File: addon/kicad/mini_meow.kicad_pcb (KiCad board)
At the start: 2 copper layers, 5 parts, among them U1 sa_connector

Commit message: pcb update, added working art files
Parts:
- added G***: LOGO, mini_meow:mini_meow_silk_lg, F.Cu at (152.2, 88.9)
- moved R1 126.5 mm to (245.0, 92.5)
- moved D1 121.1 mm to (245.0, 80.0)
- moved D2 115.1 mm to (222.5, 77.5)
- moved U1 110.8 mm to (230.0, 90.0)
- moved R2 107.3 mm to (220.0, 92.5)
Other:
- board outline added: 128.7 x 63.4 mm
- net class Default: clearance 0.2 -> 0.254; trace_width 0.25 -> 0.254; via_dia 0.6 -> 0.6858; via_drill 0.4 -> 0.3302
- rule trace_clearance: 0.2 -> 0.254

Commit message: updated library, added copper images
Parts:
- added G***: LOGO, mini_meow:mini_meow_nose, F.Cu at (148.7, 85.6)
- added G***: LOGO, mini_meow:mini_meow_necklace, F.Cu at (148.4, 99.8)
- added G***: LOGO, mini_meow:mini_meow_belly, F.Cu at (148.8, 114.0)
- moved D1 88.3 mm to (156.8, 80.7), turned to 0 degrees
- moved R2 86.3 mm to (133.7, 90.0), turned to 0 degrees
- moved D2 81.8 mm to (140.8, 80.7)
- moved U1 80.5 mm to (150.0, 99.0), turned to 180 degrees
- moved R1 80.4 mm to (164.6, 90.2), turned to 180 degrees
- moved G*** 0.18 mm to (152.1, 88.8)
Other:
- board size 128.7 x 63.4 mm -> 49.3 x 63.4 mm

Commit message: updated pcb, maybe first final draft
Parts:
- D1, D2, R1, R2, U1: moved to B.Cu
- moved R2 30.9 mm to (134.1, 120.9)
- moved R1 30.7 mm to (163.6, 120.9)
- moved U1 0.62 mm to (150.4, 98.6)
- moved G*** 0.43 mm to (148.8, 99.6)
- moved D1 0.31 mm to (156.5, 80.8)
- moved D2 0.15 mm to (140.7, 80.8)
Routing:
- net Net-(D1-Pad2): track 0.00 -> 42.2 mm
- net Net-(D2-Pad2): track 0.00 -> 41.8 mm
- net +3V3: track 0.00 -> 41.0 mm
- added copper zone on B.Cu, net GND
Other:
- board text added: "Y2F0cyBkb24ndCBoYXZlIFIxMyBsaXZlcw=="
- board text added: "dash"
- board text added: "defcon26-meow"
- board text added: "nekosurf <3"
- board text added: "tense future"

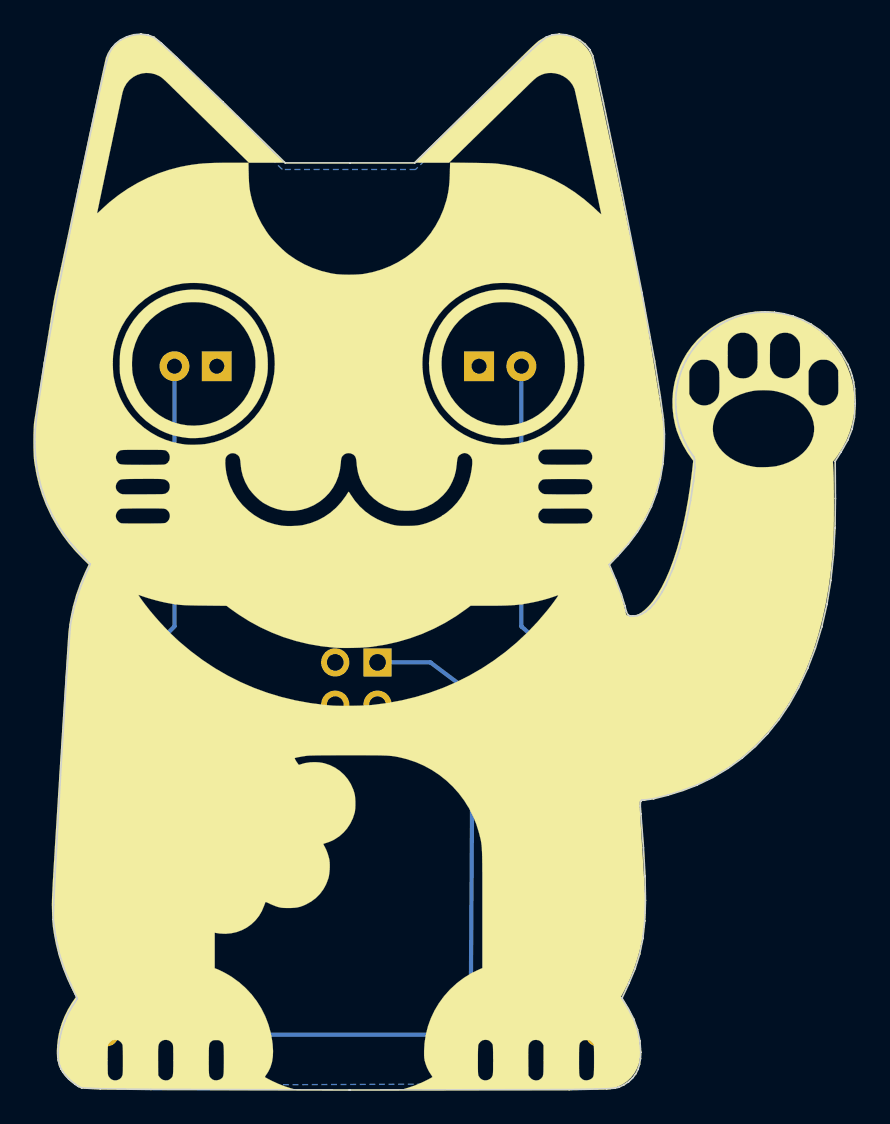
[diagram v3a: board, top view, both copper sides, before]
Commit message: updated copper layers. added ground
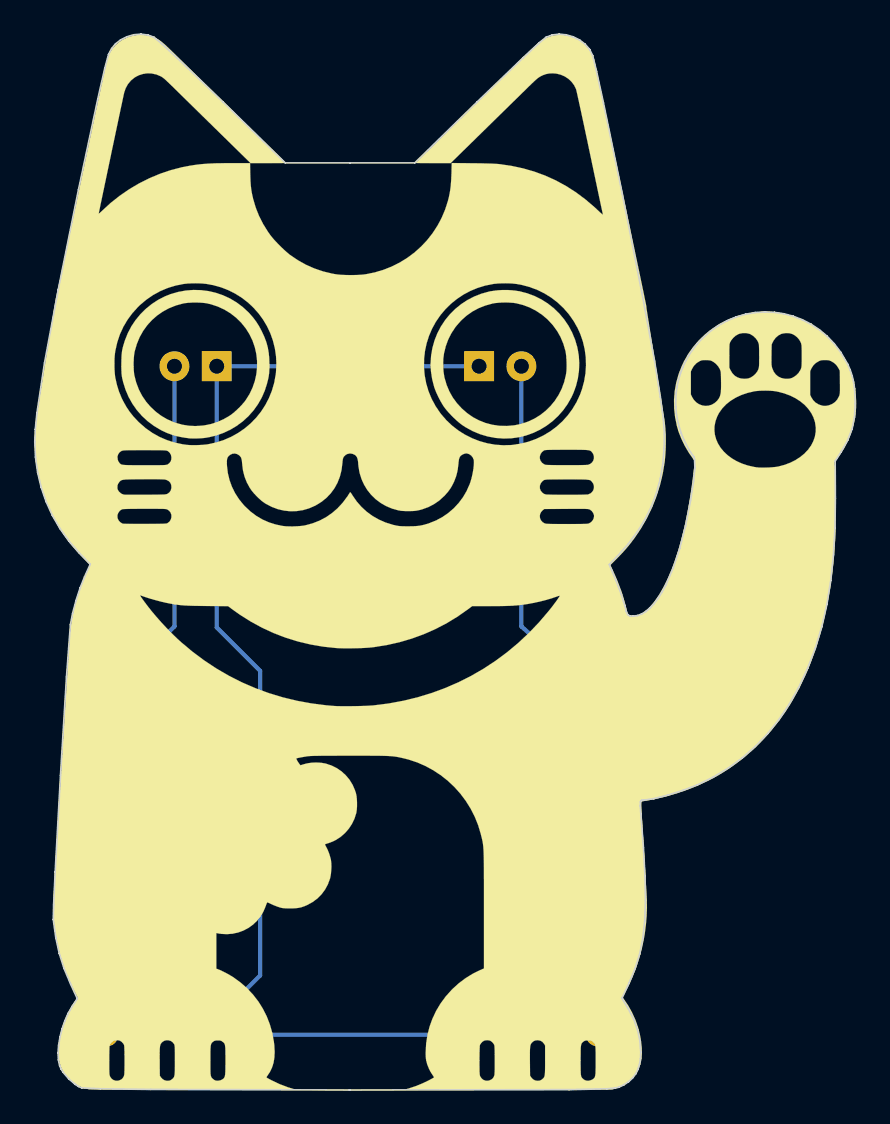
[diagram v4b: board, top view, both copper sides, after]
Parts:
- added G***: LOGO, mini_meow:heart, B.Cu at (173.6, 82.8)
- moved U1 13.7 mm to (143.3, 110.3), turned to 90 degrees
- moved G*** 1.08 mm to (148.9, 98.5)
- moved G*** 0.10 mm to (152.1, 88.8)
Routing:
- net GND: track 0.00 -> 43.8 mm
- net +3V3: track 41.0 -> 25.6 mm
- removed copper zone on B.Cu, net GND
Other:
- board text added: "nekosurf"
- board text removed: "nekosurf <3"

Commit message: updated copper layers....again...
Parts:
- moved G*** 1.13 mm to (149.2, 99.6), turned to 0 degrees
- moved G*** 0.21 mm to (149.0, 114.1)
- moved G*** 0.19 mm to (148.7, 85.4)
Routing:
- net GND: track 43.8 -> 67.9 mm
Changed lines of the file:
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@@
     (thickness 1.6)
     (drawings 221)
-    (tracks 18)
+    (tracks 20)
     (zones 0)
     (modules 10)
@@
       (xy 5.695666 -12.574343) (xy 6.06983 -12.573966)) (layer F.SilkS) (width 0.01))
   )
+  (module mini_meow:heart (layer B.Cu)
+    (at 173.609 82.804 180)
+    (fp_text reference G*** (at 0 0 180) (layer B.SilkS) hide
+      (effects (font (thickness 0.3)) (justify mirror))
+    )
+    (fp_text value LOGO (at 0.75 0 180) (layer B.SilkS) hide
+      (effects (font (thickness 0.3)) (justify mirror))
+    )
+    (fp_poly (pts (xy -0.690576 1.381518) (xy -0.548786 1.307765) (xy -0.402225 1.189289) (xy -0.344715 1.133323)
+      (xy -0.259095 1.042376) (xy -0.180277 0.951003) (xy -0.120334 0.873512) (xy -0.101701 0.845269)
+      (xy -0.062368 0.783353) (xy -0.033115 0.74457) (xy -0.024851 0.738021) (xy -0.00569 0.757723)
+      (xy 0.026022 0.807777) (xy 0.037334 0.828133) (xy 0.095374 0.913847) (xy 0.182086 1.015689)
+      (xy 0.285558 1.122043) (xy 0.393877 1.221293) (xy 0.495128 1.301823) (xy 0.572072 1.349525)
+      (xy 0.725984 1.398362) (xy 0.896095 1.410114) (xy 1.063644 1.384625) (xy 1.148611 1.35436)
+      (xy 1.287825 1.271329) (xy 1.421227 1.154973) (xy 1.531617 1.021525) (xy 1.572276 0.954474)
+      (xy 1.604083 0.888798) (xy 1.623999 0.828108) (xy 1.634662 0.757292) (xy 1.63871 0.661238)
+      (xy 1.639024 0.572072) (xy 1.635808 0.435182) (xy 1.625575 0.33177) (xy 1.605799 0.244661)
+      (xy 1.580147 0.171989) (xy 1.514945 0.030874) (xy 1.430264 -0.110054) (xy 1.322391 -0.254857)
+      (xy 1.187612 -0.407599) (xy 1.022212 -0.572343) (xy 0.822479 -0.753152) (xy 0.584697 -0.954089)
+      (xy 0.452692 -1.061512) (xy 0.322737 -1.165479) (xy 0.205672 -1.257791) (xy 0.10737 -1.333926)
+      (xy 0.033705 -1.389363) (xy -0.00945 -1.41958) (xy -0.017888 -1.423824) (xy -0.04415 -1.408527)
+      (xy -0.101634 -1.366604) (xy -0.182515 -1.304006) (xy -0.27897 -1.226685) (xy -0.305357 -1.205132)
+      (xy -0.435211 -1.098634) (xy -0.580722 -0.979255) (xy -0.722323 -0.86305) (xy -0.820734 -0.782262)
+      (xy -1.091811 -0.54456) (xy -1.313706 -0.316532) (xy -1.48693 -0.097062) (xy -1.611993 0.114969)
+      (xy -1.689408 0.320679) (xy -1.719683 0.521186) (xy -1.703329 0.717608) (xy -1.640858 0.911063)
+      (xy -1.617034 0.961194) (xy -1.538656 1.079617) (xy -1.431385 1.193412) (xy -1.310361 1.288975)
+      (xy -1.190725 1.352701) (xy -1.175169 1.358235) (xy -0.994982 1.404374) (xy -0.83638 1.412928)
+      (xy -0.690576 1.381518)) (layer B.Mask) (width 0.01))
+  )
   (module mini_meow:mini_meow_nose (layer F.Cu)
-    (at 148.7 85.6)
-    (fp_text reference G*** (at 0 0) (layer F.SilkS) hide
+    (at 148.717 85.4075)
+    (fp_text reference G*** (at 0 0) (layer F.Cu) hide
       (effects (font (thickness 0.3)))
     )
-    (fp_text value LOGO (at 0.75 0) (layer F.SilkS) hide
+    (fp_text value LOGO (at 0.75 0) (layer F.Cu) hide
       (effects (font (thickness 0.3)))
     )
@@
       (xy -1.924858 -1.183145) (xy -1.841776 -1.186452) (xy -1.735622 -1.189068) (xy -1.602989 -1.191076)
       (xy -1.440471 -1.192555) (xy -1.24466 -1.193587) (xy -1.012151 -1.194252) (xy -0.739536 -1.194632)
-      (xy -0.423409 -1.194807) (xy -0.060363 -1.194858) (xy 0 -1.19486) (xy 0.372186 -1.194811)) (layer F.Mask) (width 0.01))
+      (xy -0.423409 -1.194807) (xy -0.060363 -1.194858) (xy 0 -1.19486) (xy 0.372186 -1.194811)) (layer F.Cu) (width 0.01))
   )
   (module mini_meow:mini_meow_necklace (layer F.Cu)
-    (at 148.9075 98.4885 90)
-    (fp_text reference G*** (at 0 0 90) (layer F.SilkS) hide
+    (at 149.225 99.568)
+    (fp_text reference G*** (at 0 0) (layer F.Cu) hide
       (effects (font (thickness 0.3)))
     )
-    (fp_text value LOGO (at 0.75 0 90) (layer F.SilkS) hide
+    (fp_text value LOGO (at 0.75 0) (layer F.Cu) hide
       (effects (font (thickness 0.3)))
     )
@@
       (xy -2.289693 -2.215709) (xy -1.991288 -2.488926) (xy -1.667949 -2.719084) (xy -1.323118 -2.905262)
       (xy -0.960235 -3.04654) (xy -0.582738 -3.141996) (xy -0.19407 -3.19071) (xy 0.202331 -3.19176)
-      (xy 0.603024 -3.144227)) (layer F.Mask) (width 0.01))
+      (xy 0.603024 -3.144227)) (layer F.Cu) (width 0.01))
   )
   (module mini_meow:mini_meow_belly (layer F.Cu)
-    (at 148.85 114)
-    (fp_text reference G*** (at 0 0) (layer F.SilkS) hide
+    (at 149.0345 114.1095)
+    (fp_text reference G*** (at 0 0) (layer F.Cu) hide
       (effects (font (thickness 0.3)))
     )
-    (fp_text value LOGO (at 0.75 0) (layer F.SilkS) hide
+    (fp_text value LOGO (at 0.75 0) (layer F.Cu) hide
       (effects (font (thickness 0.3)))
     )
@@
       (xy -2.798548 -9.833833) (xy -2.656381 -9.853188) (xy -2.555255 -9.865327) (xy -2.477675 -9.871066)
       (xy -2.356242 -9.875898) (xy -2.190114 -9.879831) (xy -1.978447 -9.882872) (xy -1.720399 -9.885025)
-      (xy -1.415128 -9.886298) (xy -1.061791 -9.886698) (xy -0.659546 -9.88623)) (layer F.Mask) (width 0.01))
-  )
-  (module mini_meow:heart (layer B.Cu)
-    (at 173.609 82.804 180)
-    (fp_text reference G*** (at 0 0 180) (layer B.SilkS) hide
-      (effects (font (thickness 0.3)) (justify mirror))
-    )
-    (fp_text value LOGO (at 0.75 0 180) (layer B.SilkS) hide
-      (effects (font (thickness 0.3)) (justify mirror))
-    )
-    (fp_poly (pts (xy -0.690576 1.381518) (xy -0.548786 1.307765) (xy -0.402225 1.189289) (xy -0.344715 1.133323)
-      (xy -0.259095 1.042376) (xy -0.180277 0.951003) (xy -0.120334 0.873512) (xy -0.101701 0.845269)
-      (xy -0.062368 0.783353) (xy -0.033115 0.74457) (xy -0.024851 0.738021) (xy -0.00569 0.757723)
-      (xy 0.026022 0.807777) (xy 0.037334 0.828133) (xy 0.095374 0.913847) (xy 0.182086 1.015689)
-      (xy 0.285558 1.122043) (xy 0.393877 1.221293) (xy 0.495128 1.301823) (xy 0.572072 1.349525)
-      (xy 0.725984 1.398362) (xy 0.896095 1.410114) (xy 1.063644 1.384625) (xy 1.148611 1.35436)
-      (xy 1.287825 1.271329) (xy 1.421227 1.154973) (xy 1.531617 1.021525) (xy 1.572276 0.954474)
-      (xy 1.604083 0.888798) (xy 1.623999 0.828108) (xy 1.634662 0.757292) (xy 1.63871 0.661238)
-      (xy 1.639024 0.572072) (xy 1.635808 0.435182) (xy 1.625575 0.33177) (xy 1.605799 0.244661)
-      (xy 1.580147 0.171989) (xy 1.514945 0.030874) (xy 1.430264 -0.110054) (xy 1.322391 -0.254857)
-      (xy 1.187612 -0.407599) (xy 1.022212 -0.572343) (xy 0.822479 -0.753152) (xy 0.584697 -0.954089)
-      (xy 0.452692 -1.061512) (xy 0.322737 -1.165479) (xy 0.205672 -1.257791) (xy 0.10737 -1.333926)
-      (xy 0.033705 -1.389363) (xy -0.00945 -1.41958) (xy -0.017888 -1.423824) (xy -0.04415 -1.408527)
-      (xy -0.101634 -1.366604) (xy -0.182515 -1.304006) (xy -0.27897 -1.226685) (xy -0.305357 -1.205132)
-      (xy -0.435211 -1.098634) (xy -0.580722 -0.979255) (xy -0.722323 -0.86305) (xy -0.820734 -0.782262)
-      (xy -1.091811 -0.54456) (xy -1.313706 -0.316532) (xy -1.48693 -0.097062) (xy -1.611993 0.114969)
-      (xy -1.689408 0.320679) (xy -1.719683 0.521186) (xy -1.703329 0.717608) (xy -1.640858 0.911063)
-      (xy -1.617034 0.961194) (xy -1.538656 1.079617) (xy -1.431385 1.193412) (xy -1.310361 1.288975)
-      (xy -1.190725 1.352701) (xy -1.175169 1.358235) (xy -0.994982 1.404374) (xy -0.83638 1.412928)
-      (xy -0.690576 1.381518)) (layer B.Mask) (width 0.01))
+      (xy -1.415128 -9.886298) (xy -1.061791 -9.886698) (xy -0.659546 -9.88623)) (layer F.Cu) (width 0.01))
   )
   (gr_text Y2F0cyBkb24ndCBoYXZlIFIxMyBsaXZlcw== (at 148.336 74.422) (layer B.SilkS)
@@
   (gr_line (start 132.41897 124.01002) (end 132.220026 123.884121) (layer Edge.Cuts) (width 0.1))
   (gr_line (start 132.607035 124.095547) (end 132.41897 124.01002) (layer Edge.Cuts) (width 0.1))
-  (segment (start 156.464 80.772) (end 140.716 80.772) (width 0.254) (layer B.Cu) (net 1))
+  (segment (start 156.464 80.772) (end 156.083 107.823) (width 0.254) (layer B.Cu) (net 1))
+  (segment (start 145.161 107.7595) (end 143.3195 107.7595) (width 0.254) (layer B.Cu) (net 1))
+  (segment (start 156.083 107.823) (end 145.161 107.7595) (width 0.254) (layer B.Cu) (net 1))
   (segment (start 140.716 80.772) (end 140.716 96.4565) (width 0.254) (layer B.Cu) (net 1))
   (segment (start 143.3195 99.06) (end 143.3195 107.7595) (width 0.254) (layer B.Cu) (net 1))

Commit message: updated some silkscreen text
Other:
- board text added: "+"
- board text added: "-"
- board text added: "GND"
- board text added: "MEOW EMWO OWME WOEM"
- board text added: "VCC"
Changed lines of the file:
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@@
     (links 6)
     (no_connects 0)
-    (area 129.545923 60.619632 179.358787 124.630237)
+    (area 129.545923 60.619632 179.358787 124.739737)
     (thickness 1.6)
-    (drawings 221)
+    (drawings 228)
     (tracks 20)
     (zones 0)
@@
   (page A4)
   (layers
-    (0 F.Cu signal)
+    (0 F.Cu signal hide)
     (31 B.Cu signal)
     (32 B.Adhes user)
@@
     (descr "LED, diameter 5.0mm, 2 pins, http://cdn-reichelt.de/documents/datenblatt/A500/LL-504BC2E-009.pdf")
     (tags "LED diameter 5.0mm 2 pins")
-    (fp_text reference D1 (at 1.27 3.96) (layer B.SilkS)
+    (fp_text reference D1 (at 1.27 4.2545) (layer B.SilkS)
       (effects (font (size 1 1) (thickness 0.15)) (justify mirror))
     )
@@
       (xy -1.415128 -9.886298) (xy -1.061791 -9.886698) (xy -0.659546 -9.88623)) (layer F.Cu) (width 0.01))
   )
+  (gr_text "MEOW\nEMWO\nOWME\nWOEM\n" (at 173.355 91.948) (layer B.SilkS)
+    (effects (font (size 1 1) (thickness 0.2)) (justify mirror))
+  )
+  (gr_text VCC (at 147.066 112.7125) (layer B.SilkS)
+    (effects (font (size 1 1) (thickness 0.2)) (justify mirror))
+  )
+  (gr_text GND (at 147.2565 106.2355) (layer B.SilkS)
+    (effects (font (size 1 1) (thickness 0.2)) (justify mirror))
+  )
+  (gr_text + (at 160.2105 84.963) (layer B.SilkS)
+    (effects (font (size 1.5 1.5) (thickness 0.3)) (justify mirror))
+  )
+  (gr_text + (at 137.033 84.8995) (layer B.SilkS)
+    (effects (font (size 1.5 1.5) (thickness 0.3)) (justify mirror))
+  )
+  (gr_text - (at 155.1305 84.963) (layer B.SilkS)
+    (effects (font (size 1.5 1.5) (thickness 0.3)) (justify mirror))
+  )
+  (gr_text - (at 141.986 84.836) (layer B.SilkS)
+    (effects (font (size 1.5 1.5) (thickness 0.3)) (justify mirror))
+  )
   (gr_text Y2F0cyBkb24ndCBoYXZlIFIxMyBsaXZlcw== (at 148.336 74.422) (layer B.SilkS)

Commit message: updated mask for copper
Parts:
- removed the G*** at (173.6, 82.8)
- added G***: LOGO, mini_meow:mini_meow_nose_mask, F.Cu at (148.7, 85.3)
- added G***: LOGO, mini_meow:heartx, B.Cu at (173.5, 82.7)
- added G***: LOGO, mini_meow:mini_meow_collar_mask, F.Cu at (149.3, 99.6)
- added G***: LOGO, mini_meow:mini_meow_belly_mask, F.Cu at (149.0, 114.0)
- G***: footprint mini_meow:mini_meow_necklace -> mini_meow:mini_meow_collar
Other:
- net class Default: trace_width 0.254 -> 0.381
